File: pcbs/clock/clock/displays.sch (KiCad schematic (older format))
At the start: 48 parts, among them Q10 BSS138, Q11 BSS138, Q12 BSS138, Q3 BSS138, Q4 BSS138, Q5 BSS138, Q6 BSS138, Q7 BSS138, Q8 BSS138, Q9 BSS138, U10 KCSC02-105, U11 KCSC02-105, U12 KCSC02-105, U13 KCSC02-105, U14 KCSC02-105, U15 KCSC02-105, U16 KCSC02-105, U7 KCSC02-105, U8 KCSC02-105, U9 KCSC02-105

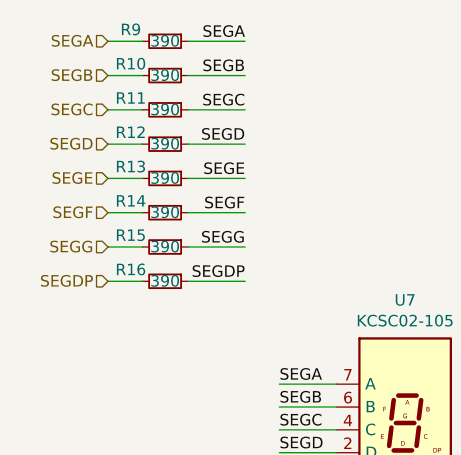
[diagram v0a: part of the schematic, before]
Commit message: Rough clock layout.
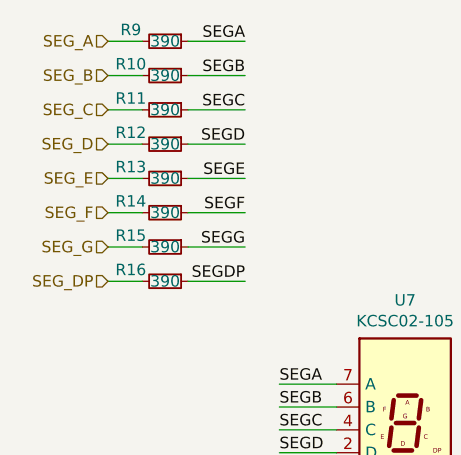
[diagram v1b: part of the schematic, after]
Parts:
- R10, R11, R12, R13, R14, R15, R16, R17, R18, R19, R20, R21, R22, R23, R24, R25, R26, R27, R28, R29, R30, R31, R32, R33, R34, R35, R36, R9: footprint (none) -> Resistor_SMD:R_0603_1608Metric
- U10, U11, U12, U13, U14, U15, U16, U7, U8, U9: footprint Display_7Segment:KCSC02-105 -> Display_7Segment:7SegmentLED_LTS6760_LTS6780
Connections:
- net SEGA: no longer R9.2
- net SEGB: no longer R10.2
- net SEGC: no longer R11.2
- net SEGD: no longer R12.2
- net SEGDP: no longer R16.2
- net SEGE: no longer R13.2
- net SEGF: no longer R14.2
- net SEGG: no longer R15.2
- new net SEG_A: R9.2
- new net SEG_B: R10.2
- new net SEG_C: R11.2
- new net SEG_D: R12.2
- new net SEG_DP: R16.2
- new net SEG_E: R13.2
- new net SEG_F: R14.2
- new net SEG_G: R15.2
